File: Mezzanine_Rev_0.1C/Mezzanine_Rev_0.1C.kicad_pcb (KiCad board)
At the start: 2 copper layers, 170 x 84.8 mm, 51 parts, among them J1 QBUS_DWK_64Pin_MBT, J2 DIP20 Header, J3 DIP20 Header, J4 IDC-64M, J5 IDC-16M, J6 IDC-20M, J7 Conn_01x03_Pin, J8 Conn_01x07_Pin, U1 1533LI1, U10 74LS07, U11 74LS74, U2 1533TM2, U3 1533LA8, U4 CD74HCT4067M, U5 1533LE4, U6 1533AP6, U7 1533AP6, U8 74LS07, U9 74LS07

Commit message: Mezzanine: Board layout
Completed layout, to be verified and refined if needed.
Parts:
- added C11: 0.1uF, Capacitor_THT:C_Disc_D6.0mm_W2.5mm_P5.00mm, F.Cu at (147.6, 77.3)
- added C12: 0.1uF, Capacitor_THT:C_Disc_D6.0mm_W2.5mm_P5.00mm, F.Cu at (182.4, 116.4)
- added C13: 0.1uF, Capacitor_THT:C_Disc_D6.0mm_W2.5mm_P5.00mm, F.Cu at (180.9, 89.6)
- added C14: 0.1uF, Capacitor_THT:C_Disc_D6.0mm_W2.5mm_P5.00mm, F.Cu at (179.5, 59.5)
- added C15: 0.1uF, Capacitor_THT:C_Disc_D6.0mm_W2.5mm_P5.00mm, F.Cu at (197.3, 96.0)
- added C16: 0.1uF, Capacitor_THT:C_Disc_D6.0mm_W2.5mm_P5.00mm, F.Cu at (197.6, 85.6)
- added C17: 0.1uF, Capacitor_THT:C_Disc_D6.0mm_W2.5mm_P5.00mm, F.Cu at (195.8, 75.9)
- added C18: 0.1uF, Capacitor_THT:C_Disc_D6.0mm_W2.5mm_P5.00mm, F.Cu at (184.9, 59.5)
- added C19: 0.1uF, Capacitor_THT:C_Disc_D6.0mm_W2.5mm_P5.00mm, F.Cu at (197.9, 106.0)
- added C20: 0.1uF, Capacitor_THT:C_Disc_D6.0mm_W2.5mm_P5.00mm, F.Cu at (146.5, 63.0)
- added R7: 2.2K, Resistor_THT:R_Axial_DIN0204_L3.6mm_D1.6mm_P7.62mm_Horizontal, F.Cu at (146.5, 110.1)
- J8: value Conn_01x07_Pin -> Conn_01x16_Pin; footprint Connector_PinHeader_2.54mm:PinHeader_1x06_P2.54mm_Horizontal -> Connector_PinHeader_2.54mm:PinHeader_1x16_P2.54mm_Horizontal
- R6: footprint Resistor_THT:R_Axial_DIN0204_L3.6mm_D1.6mm_P7.62mm_Horizontal -> Resistor_THT:R_Axial_DIN0207_L6.3mm_D2.5mm_P7.62mm_Horizontal
- U4: footprint Package_SO:SOIC-24W_7.5x15.4mm_P1.27mm -> Package_DIP:DIP-24_W15.24mm
- moved R3 127.5 mm to (103.7, 111.2), turned to 180 degrees
- moved C9 126.2 mm to (144.3, 84.7), turned to 180 degrees
- moved U11 124.4 mm to (131.1, 72.8), turned to 90 degrees
- moved R1 117.6 mm to (195.0, 84.6), turned to -90 degrees
- moved C10 117.2 mm to (154.2, 114.7)
- moved U5 112.2 mm to (200.7, 113.4), turned to 90 degrees
- moved J7 111.3 mm to (136.8, 75.7), turned to -90 degrees
- moved U1 107.9 mm to (200.7, 102.6), turned to 90 degrees
- moved R2 105.8 mm to (195.6, 73.6), turned to 180 degrees
- moved C8 96.8 mm to (132.6, 111.5), turned to 180 degrees
- moved U2 94.3 mm to (200.7, 91.8), turned to 90 degrees
- moved R6 86.6 mm to (128.3, 83.8), turned to 90 degrees
- moved C7 86.2 mm to (120.5, 109.6), turned to 180 degrees
- moved U3 81.2 mm to (200.7, 81.1), turned to 90 degrees
- moved C4 79.5 mm to (91.9, 83.9), turned to 180 degrees
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- renumbered D6 to DD6, D7 to DD7
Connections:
- DD1 pad 13: /~{EXT_IRQ2} -> ~{EXT_IRQ2}
- DD1 pad 6: /~{CPU_RPLY} -> ~{CPU_RPLY}
- DD10 pad 11: /~{CPU_DIN} -> ~{CPU_DIN}
- DD10 pad 14: /~{EXT_SYNC} -> ~{EXT_SYNC}
- DD10 pad 4: /~{EXT_WTBT} -> ~{EXT_WTBT}
- DD10 pad 5: /~{CPU_DOUT} -> ~{CPU_DOUT}
- DD10 pad 7: ~{DOUT} -> /~{DOUT}
- DD2 pad 10: /~{EXT_VIRQ} -> ~{EXT_VIRQ}
- DD3 pad 3: /~{EXT_DMG} -> ~{EXT_DMG}
- DD4 pad 10: /~{ROM_DIN} -> ~{ROM_DIN}
- J1 pad 24: ~{DOUT} -> /~{DOUT}
- J8 pad 1: ~{LOCK} -> Net-(J8-Pin_1)
- J8 pad 2: SYSRAM -> Net-(J8-Pin_2)
- J8 pad 3: ~{DOUT} -> ~{EXT_VIRQ}
- J8 pad 4: SEL1 -> ~{CPU_RPLY}
- J8 pad 5: CPU_DIN -> ~{ROM_DIN}
- J8 pad 6: Net-(J8-Pin_6) -> ~{EXT_IRQ2}
- RN1 pad 10: /~{BDAL8} -> /~{BSACK}
- RN1 pad 6: /~{BEVNT} -> /~{BDAL11}
- RN1 pad 7: /~{BDAL10} -> /~{BEVNT}
- RN1 pad 8: /~{BDAL9} -> /~{BDAL10}
- RN1 pad 9: /~{BSACK} -> /~{BDAL9}
- RN2 pad 10: /BPOK -> /~{BIRQ3}
- RN2 pad 2: /~{BDAL7} -> /~{BDAL8}
- RN2 pad 3: /~{BDAL6} -> /~{BDAL7}
- RN2 pad 4: /~{BDAL5} -> /~{BDAL6}
- RN2 pad 5: /~{BDAL4} -> /~{BDAL5}
- RN2 pad 6: /~{BDAL3} -> /~{BDAL4}
- RN2 pad 7: /SSpare7 -> /~{BDAL3}
- RN2 pad 8: /~{BDAL2} -> /SSpare7
- RN2 pad 9: /~{BIRQ3} -> /~{BDAL2}
- RN3 pad 10: /~{BIAKO} -> /~{BBS7}
- RN3 pad 2: /BDCOK -> /BPOK
- RN3 pad 3: /~{BDAL1} -> /BDCOK
- RN3 pad 4: /~{BDAL0} -> /~{BDAL1}
- RN3 pad 5: /~{BINIT} -> /~{BDAL0}
- RN3 pad 6: /~{BDMGO} -> /~{BINIT}
- RN3 pad 7: /~{BDMGI} -> /~{BDMGO}
- RN3 pad 8: /~{BBS7} -> /~{BDMGI}
- RN4 pad 10: /~{BDOUT} -> /~{BDMR}
- RN4 pad 2: /~{BDMR} -> /~{BRPLY}
- RN4 pad 3: /~{BIAKI} -> /~{BDIN}
- RN4 pad 4: /~{BIRQ4} -> /SRUN
- RN4 pad 5: /~{BWTBT} -> /~{BSYNC}
- RN4 pad 6: /~{BSYNC} -> /~{BWTBT}
- RN4 pad 7: /~{BDIN} -> /~{BIRQ4}
- RN4 pad 8: /SRUN -> /~{BIAKI}
- RN4 pad 9: /~{BRPLY} -> /~{BIAKO}
- U10 pad 1: /~{A12} -> /~{M3}
- U10 pad 10: Net-(J6-Pin_17) -> /~{IA14}
- U10 pad 11: /~{M2} -> /~{A14}
- U10 pad 12: Net-(J6-Pin_19) -> Net-(J6-Pin_17)
- U10 pad 13: /~{M3} -> /~{M2}
- U10 pad 2: /~{IA12} -> Net-(J6-Pin_19)
- U10 pad 3: /~{A13} -> /~{A15}
- U10 pad 4: /~{IA13} -> /~{IA15}
- U10 pad 5: /~{A14} -> /~{A13}
- U10 pad 6: /~{IA14} -> /~{IA13}
- U10 pad 8: /~{IA15} -> /~{IA12}
- U10 pad 9: /~{A15} -> /~{A12}
- U11 pad 14: (no net) -> VCC
- U11 pad 5: Net-(J8-Pin_6) -> Net-(J8-Pin_1)
- U11 pad 6: Net-(J8-Pin_7) -> Net-(J8-Pin_2)
- U11 pad 7: (no net) -> GND
- U8 pad 1: /~{A0} -> /~{A5}
- U8 pad 10: /~{IA4} -> /~{IA2}
- U8 pad 11: /~{A4} -> /~{A2}
- U8 pad 12: /~{IA5} -> /~{IA4}
- U8 pad 13: /~{A5} -> /~{A4}
- U8 pad 2: /~{IA0} -> /~{IA5}
- U8 pad 3: /~{A1} -> /~{A3}
- U8 pad 4: /~{IA1} -> /~{IA3}
- U8 pad 5: /~{A2} -> /~{A1}
- U8 pad 6: /~{IA2} -> /~{IA1}
- U8 pad 8: /~{IA3} -> /~{IA0}
- U8 pad 9: /~{A3} -> /~{A0}
- U9 pad 1: /~{A6} -> /~{A11}
- U9 pad 10: /~{IA10} -> /~{IA8}
- U9 pad 11: /~{A10} -> /~{A8}
- U9 pad 12: /~{IA11} -> /~{IA10}
- U9 pad 13: /~{A11} -> /~{A10}
- U9 pad 2: /~{IA6} -> /~{IA11}
- U9 pad 3: /~{A7} -> /~{A9}
- U9 pad 4: /~{IA7} -> /~{IA9}
- U9 pad 5: /~{A8} -> /~{A7}
- U9 pad 6: /~{IA8} -> /~{IA7}
- U9 pad 8: /~{IA9} -> /~{IA6}
- U9 pad 9: /~{A9} -> /~{A6}
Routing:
- net /~{AD2}: track 0.00 -> 254.0 mm, vias 0 -> 1
- net /~{AD3}: track 0.00 -> 245.1 mm, vias 0 -> 1
- net /~{INIT}: track 0.00 -> 205.2 mm, vias 0 -> 1
- net GND: track 0.00 -> 204.5 mm, vias 0 -> 1
- net /~{A9}: track 0.00 -> 186.4 mm
- net /~{A6}: track 0.00 -> 180.1 mm, vias 0 -> 1
- net /~{A7}: track 0.00 -> 178.3 mm
- net /~{A15}: track 0.00 -> 154.2 mm, vias 0 -> 1
- net /~{A14}: track 0.00 -> 153.7 mm, vias 0 -> 2
- net /~{A13}: track 0.00 -> 143.8 mm, vias 0 -> 1
- net /~{A0}: track 0.00 -> 137.6 mm
- net /~{A2}: track 0.00 -> 137.0 mm
- net /~{A11}: track 0.00 -> 136.8 mm
- net /~{A4}: track 0.00 -> 136.6 mm
- net /~{A8}: track 0.00 -> 136.3 mm
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- added copper zone on B.Cu, net GND
- added copper zone on F.Cu, net VCC
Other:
- board size 170 x 84.8 mm -> 170 x 85.1 mm

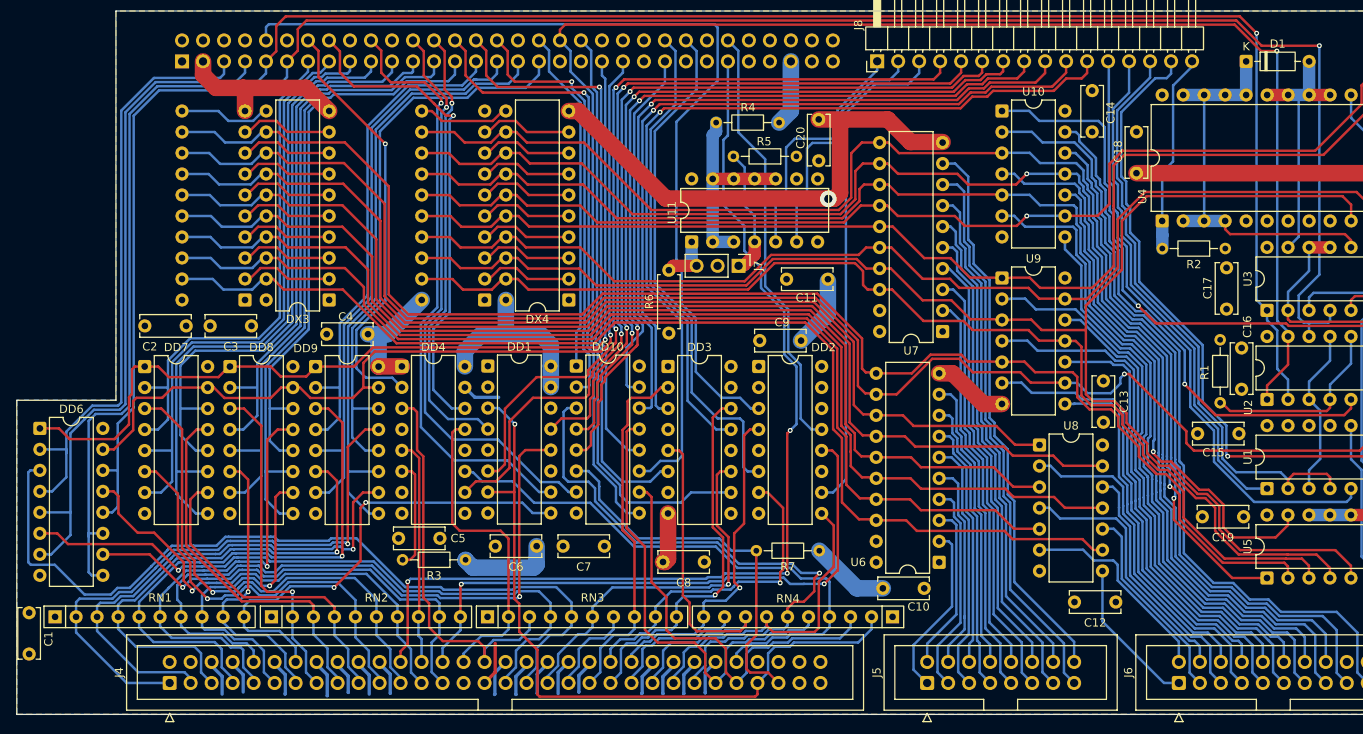
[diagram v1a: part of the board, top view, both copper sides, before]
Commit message: Mezzanine: Improve layout
More power connections, rearranged resistors.
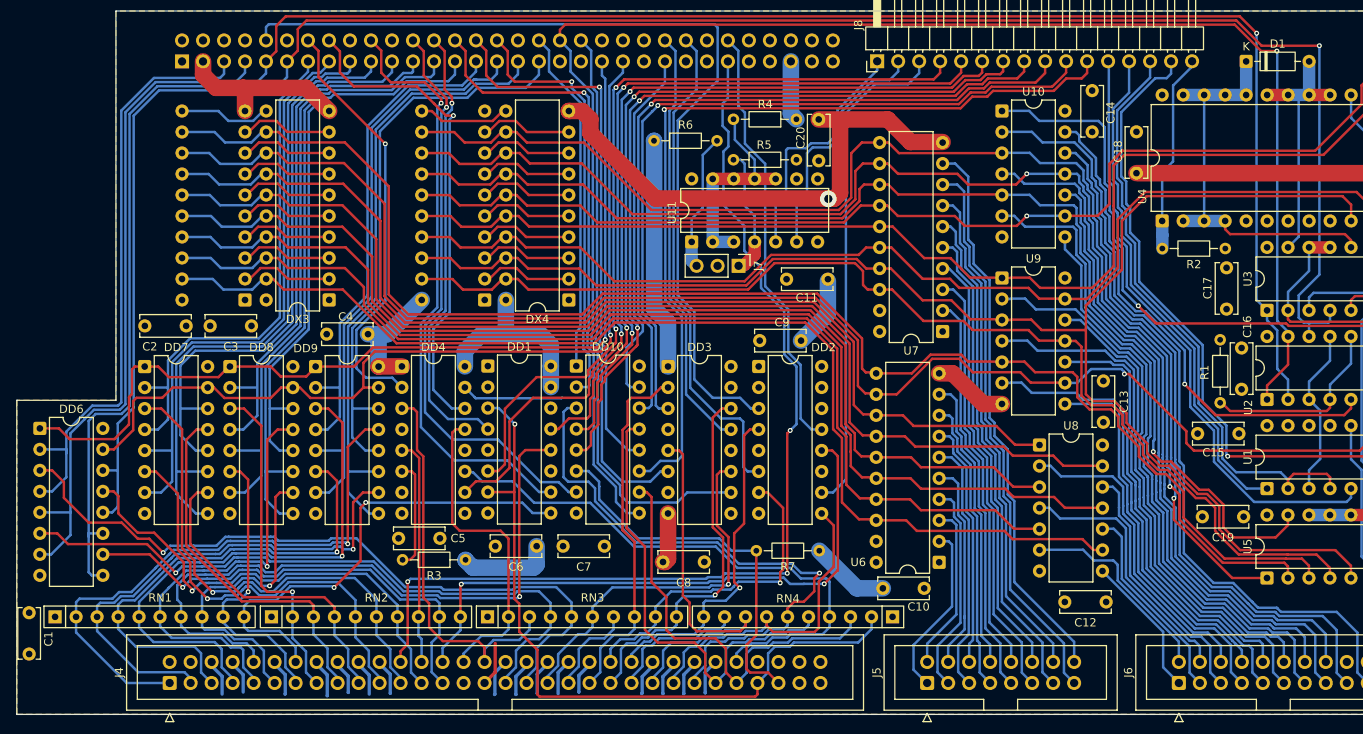
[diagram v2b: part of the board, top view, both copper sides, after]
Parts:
- R6: footprint Resistor_THT:R_Axial_DIN0207_L6.3mm_D2.5mm_P7.62mm_Horizontal -> Resistor_THT:R_Axial_DIN0204_L3.6mm_D1.6mm_P7.62mm_Horizontal
- moved R6 23.3 mm to (126.5, 60.5), turned to 0 degrees
- moved R4 2.13 mm to (143.8, 57.9)
- moved C12 1.17 mm to (181.2, 116.3)
- moved R5 0.41 mm to (143.8, 62.8)
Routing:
- net VCC: track 84.9 -> 112.2 mm
- net /~{BDAL0}: track 98.6 -> 86.4 mm, vias 0 -> 1
- net Net-(J7-Pin_3): track 6.70 -> 16.6 mm
- net GND: track 204.5 -> 213.2 mm
- net /~{BS7}: track 53.9 -> 51.7 mm
- net /~{IRQ1}: track 62.3 -> 60.2 mm
- net ~{CPU_DIN}: track 105.0 -> 103.2 mm
- net Net-(U11A-C): track 24.8 -> 26.0 mm
- net /~{IA0}: track 18.4 -> 17.4 mm
- net /~{A6}: track 180.1 -> 179.3 mm
- net /50Hz: track 122.7 -> 123.3 mm
- net /~{DMR}: track 110.7 -> 111.2 mm

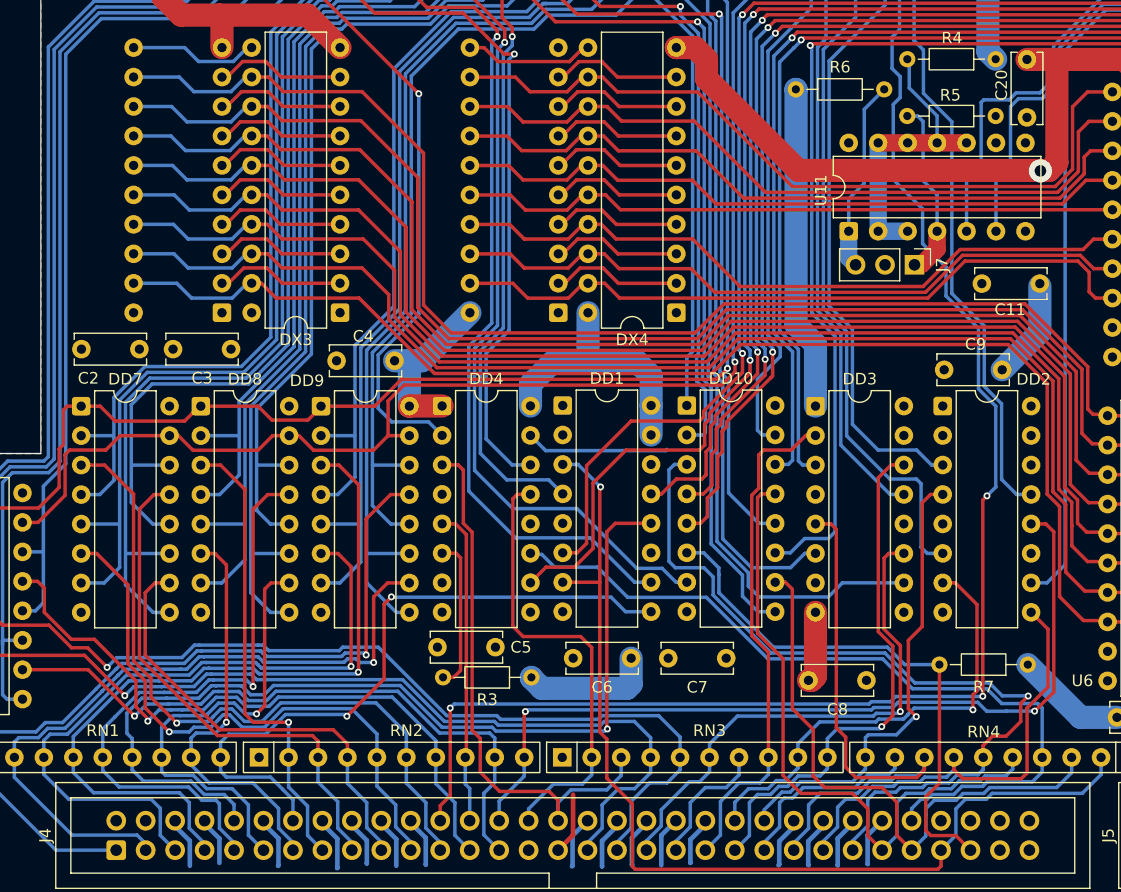
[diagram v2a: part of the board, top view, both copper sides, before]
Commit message: Mezzanine: More power improvements
More connectivity
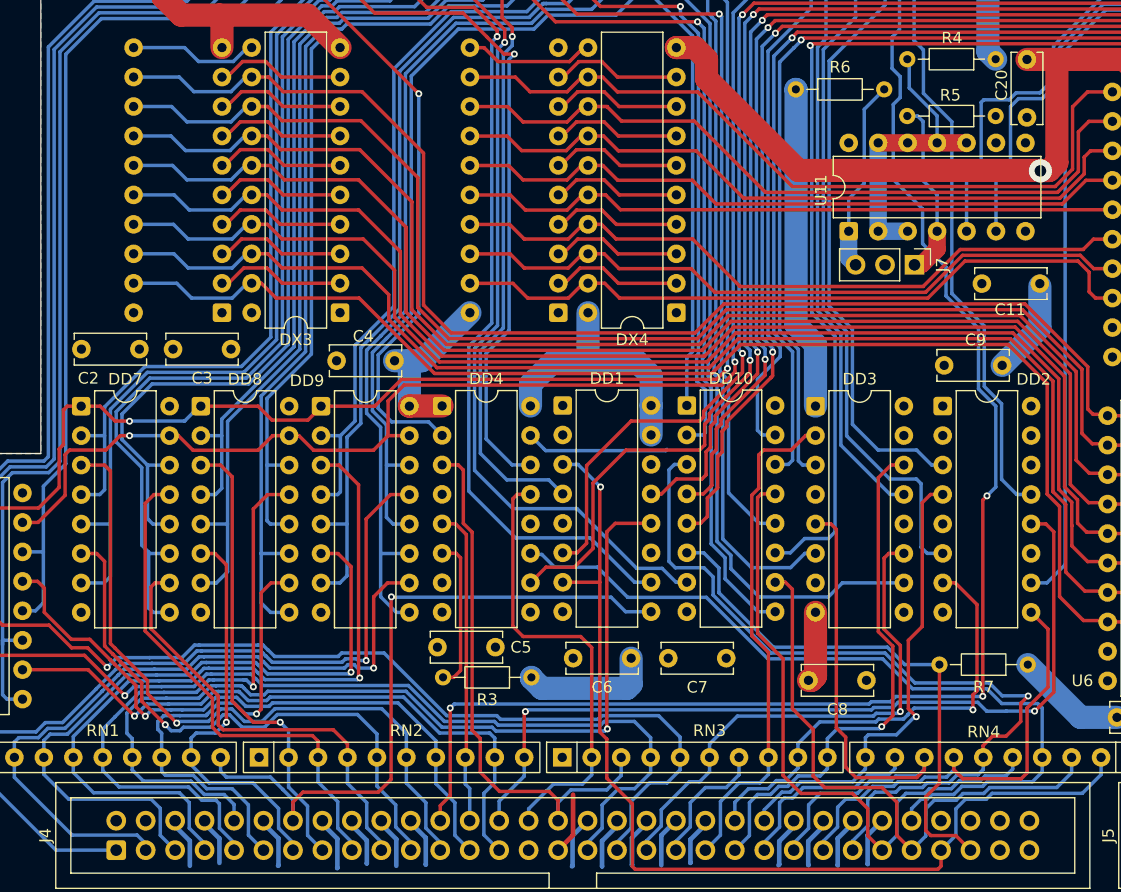
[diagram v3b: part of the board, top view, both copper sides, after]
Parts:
- moved C9 0.38 mm to (144.3, 84.3)
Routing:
- net /~{AD9}: track 71.5 -> 69.8 mm
- net /~{AD10}: track 75.4 -> 73.7 mm
- net /~{AD11}: track 69.0 -> 67.4 mm
- net /~{AD8}: track 61.1 -> 59.5 mm
- net /~{BSACK}: track 58.3 -> 59.8 mm, vias 2 -> 1
- net /~{AD15}: track 69.1 -> 67.8 mm
- net /~{AD6}: track 76.5 -> 75.2 mm
- net /~{AD12}: track 60.1 -> 58.9 mm
- net /~{AD14}: track 75.2 -> 74.0 mm
- net /~{AD13}: track 70.9 -> 69.8 mm
- net /~{BDAL3}: track 57.0 -> 55.9 mm
- net /~{BDAL12}: track 65.6 -> 66.5 mm
- net /~{BDAL14}: track 60.5 -> 61.3 mm
- net /~{AD5}: track 70.9 -> 70.2 mm
- net Net-(DD6A-CB): track 109.2 -> 110.0 mm, vias 1 -> 2
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
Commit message: Mezzanine: Change J8
Use dual-row angular connector, actually possible to use IDC-16. Gives way to
main board's oscillator and also allows for crimping on the cable.
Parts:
- J8: value Conn_01x16_Pin -> PLD-16R; footprint Connector_PinHeader_2.54mm:PinHeader_1x16_P2.54mm_Horizontal -> Connector_PinHeader_2.54mm:PinHeader_2x08_P2.54mm_Horizontal
- moved C14 8.38 mm to (185.3, 53.4), turned to 180 degrees
- moved C20 5.02 mm to (146.6, 57.9), turned to -90 degrees
- moved J8 1.73 mm to (151.8, 50.9)
- moved C18 1.67 mm to (184.9, 57.8)
- moved C11 1.65 mm to (145.9, 77.2), turned to 0 degrees
- moved D1 1.56 mm to (198.2, 52.5)
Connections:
- J8 pad 10: ~{EXT_DMG} -> ~{EXT_SYNC}
- J8 pad 11: ~{CPU_DIN} -> CPU_DIN
- J8 pad 12: CPU_DIN -> ~{CPU_DIN}
- J8 pad 3: ~{EXT_VIRQ} -> ~{CPU_RPLY}
- J8 pad 4: ~{CPU_RPLY} -> ~{EXT_VIRQ}
- J8 pad 5: ~{ROM_DIN} -> ~{EXT_IRQ2}
- J8 pad 6: ~{EXT_IRQ2} -> ~{ROM_DIN}
- J8 pad 7: ~{EXT_WTBT} -> ~{CPU_DOUT}
- J8 pad 8: ~{CPU_DOUT} -> ~{EXT_WTBT}
- J8 pad 9: ~{EXT_SYNC} -> ~{EXT_DMG}
- U11 pad 5: Net-(J8-Pin_1) -> Net-(J8-Pin_2)
- U11 pad 6: Net-(J8-Pin_2) -> Net-(J8-Pin_1)
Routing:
- net ~{EXT_DMG}: track 91.8 -> 77.4 mm
- net ~{LOCK}: track 23.5 -> 37.6 mm
- net CPU_DIN: track 73.5 -> 86.3 mm
- net ~{CPU_DIN}: track 103.2 -> 90.6 mm
- net ~{CPU_DOUT}: track 96.1 -> 84.3 mm
- net SEL1: track 73.1 -> 84.4 mm
- net ~{EXT_SYNC}: track 90.0 -> 80.0 mm
- net DOUT: track 61.7 -> 71.6 mm
- net ~{EXT_IRQ2}: track 92.1 -> 82.8 mm
- net ~{EXT_WTBT}: track 91.7 -> 84.3 mm
- net VCC: track 111.8 -> 118.8 mm
- net ~{CPU_RPLY}: track 98.6 -> 91.7 mm
- net SYSRAM: track 79.0 -> 84.7 mm
- net ~{ROM_DIN}: track 105.4 -> 100.6 mm
- net /~{AD2}: track 254.0 -> 258.6 mm
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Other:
- outline, holes or cut-outs redrawn

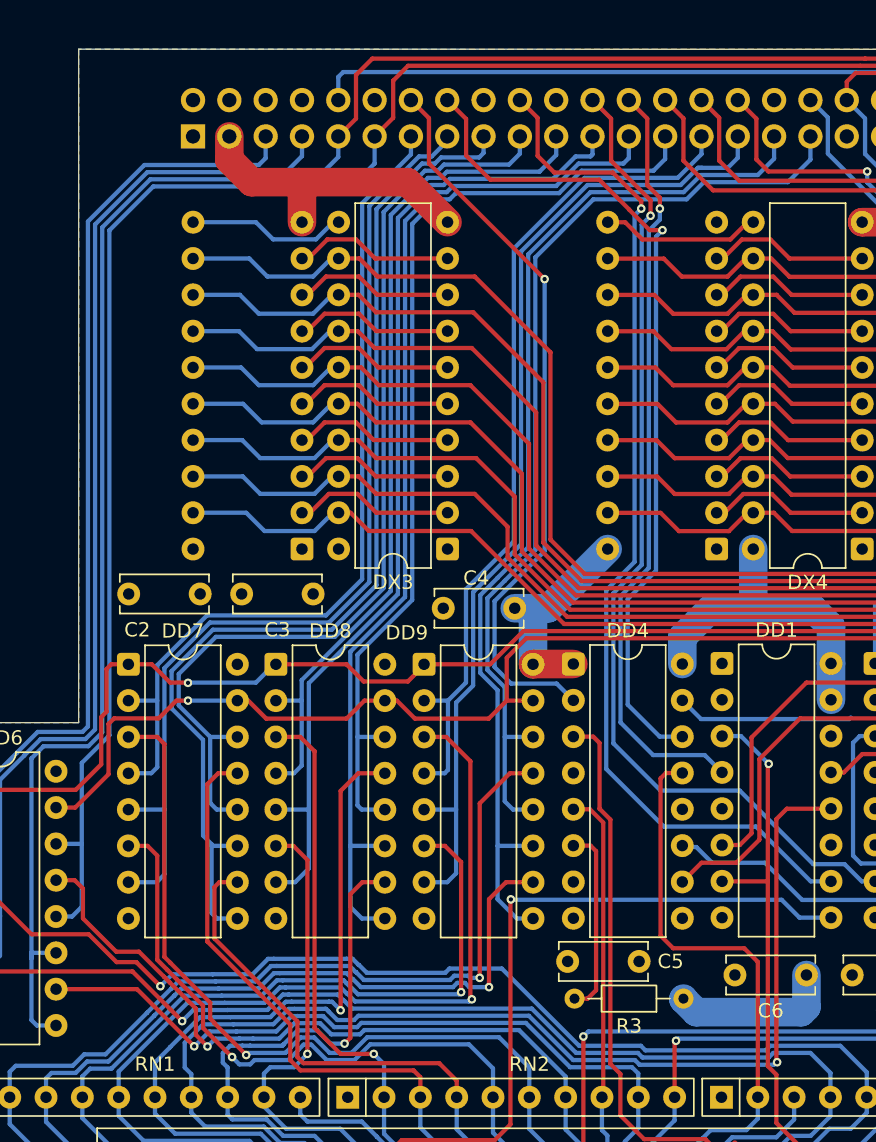
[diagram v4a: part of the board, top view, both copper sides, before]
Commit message: Mezzanine: Fix address bus connector placement
Distance from main connector should be 5mm, not 6
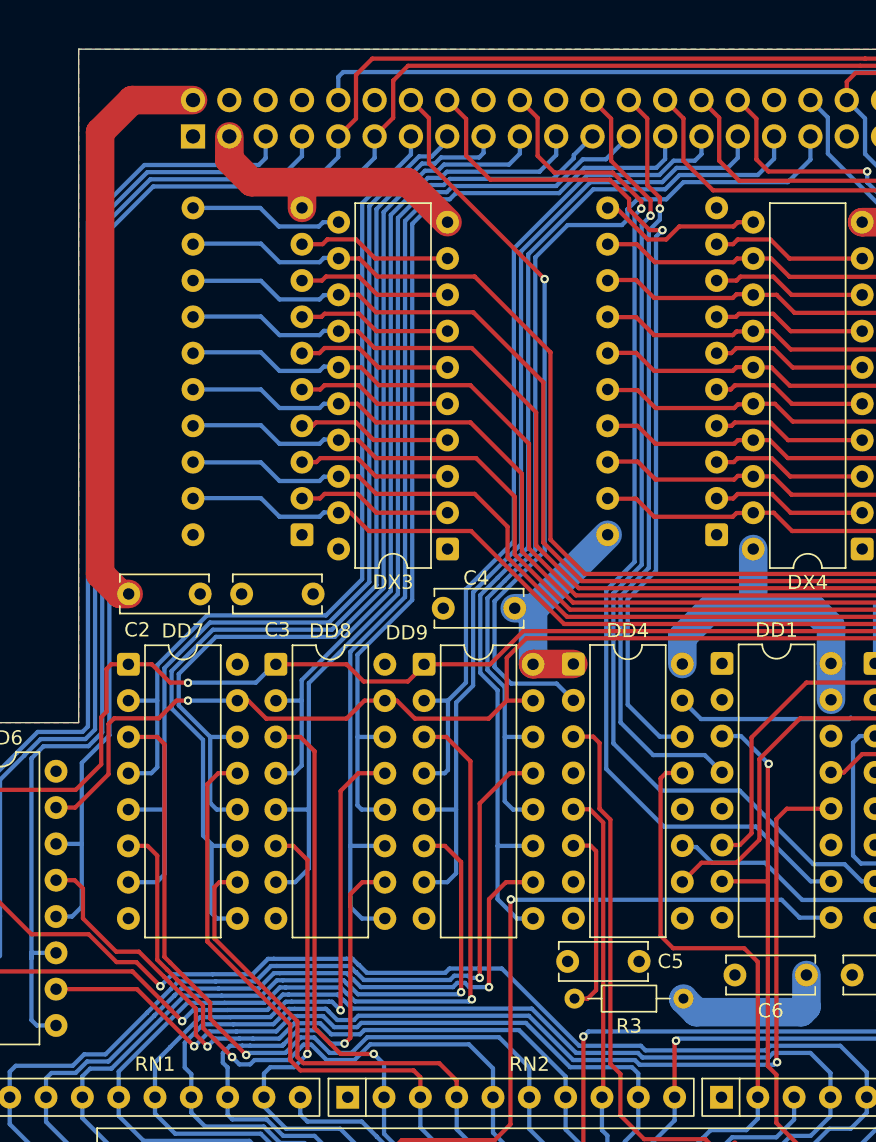
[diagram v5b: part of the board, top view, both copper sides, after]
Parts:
- moved J2 1.00 mm to (77.0, 78.8)
- moved J3 1.00 mm to (106.0, 78.8)
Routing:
- net GND: track 209.5 -> 249.4 mm
- net /~{AD10}: track 73.7 -> 72.8 mm
- net /~{AD9}: track 69.8 -> 69.2 mm
